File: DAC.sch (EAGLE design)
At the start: 89 parts, among them IC1 LM2662, IC2 PCM1793, IC3 OPA2134PA, IC4 LMH6643, J1 USBSMD, J2 RCJ-21XXMILL, U1 LDO-TPS78233, U2 PCM2707, Y1 12MHz/20pF

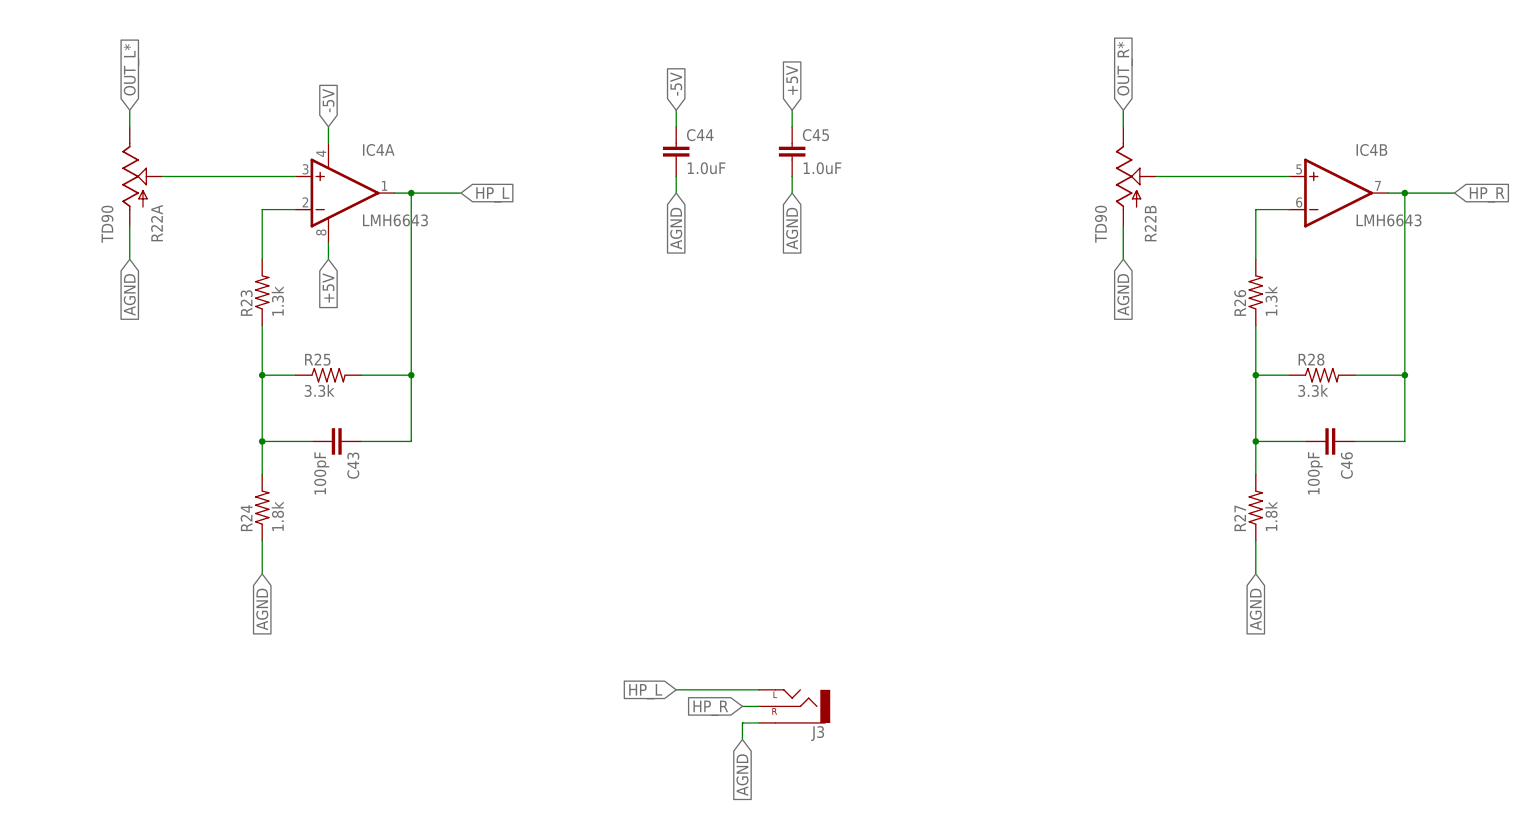
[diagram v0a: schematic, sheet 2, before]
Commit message: More decoupling
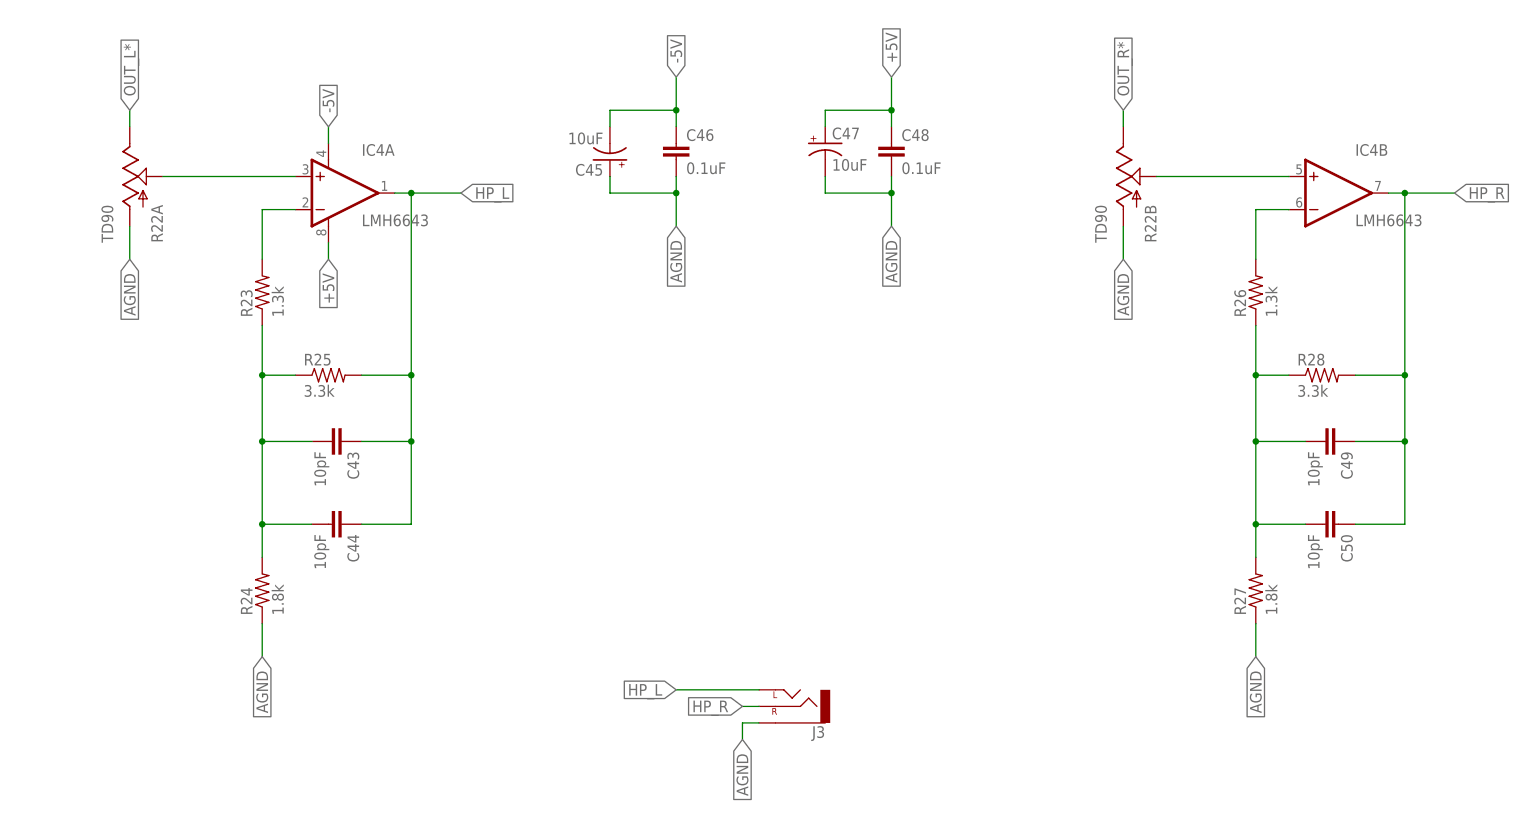
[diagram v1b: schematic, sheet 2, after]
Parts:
- added C47: 10uF, SparkFun-Capacitors:CAP_POLPTH2
- added C48: 0.1uF, SparkFun-Capacitors:1.0UF-16V-10%(0603)
- added C49: 10pF, SparkFun-Capacitors:CAPPTH
- added C50: 10pF, SparkFun-Capacitors:10PF-50V-5%(0603)
- C43: value 100pF -> 10pF
- C44: value 1.0uF -> 10pF; device SparkFun-Capacitors:1.0UF-16V-10%(0603) -> SparkFun-Capacitors:10PF-50V-5%(0603)
- C45: value 1.0uF -> 10uF; device SparkFun-Capacitors:1.0UF-16V-10%(0603) -> SparkFun-Capacitors:CAP_POLPTH2
- C46: value 100pF -> 0.1uF; device SparkFun-Capacitors:CAPPTH -> SparkFun-Capacitors:1.0UF-16V-10%(0603)
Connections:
- net +5V: now also C47.+, C48.1; no longer C45.1
- net -5V: now also C45.-, C46.1; no longer C44.1
- net AGND: now also C45.+, C46.2, C47.-, C48.2; no longer C44.2, C45.2
- net HP_L: now also C44.1
- net HP_R: now also C49.1, C50.1; no longer C46.1
- net N$14: now also C44.2
- net N$19: now also C49.2, C50.2; no longer C46.2
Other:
- note added: "Optional"
- moved on the sheet: C44, C46, R24, R27

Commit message: Caps footprint changed to more standard
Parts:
- C18, C21, C22, C6: device rcl:CPOL-USE3.5-8 -> my-cap:CAP_POLPTH8MM
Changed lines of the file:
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@@
 <attribute name="MOUSER_ID" value=" 652-SRN6045-101M"/>
 </part>
-<part name="C21" library="rcl" deviceset="CPOL-US" device="E3.5-8" value="220uF">
+<part name="C21" library="my-cap" deviceset="CAP_POL" device="PTH8MM" value="220uF">
 <attribute name="PACKAGE" value="8/3.5"/>
 </part>
@@
 <part name="C15" library="SparkFun-Capacitors" deviceset="0.1UF-25V-5%(0603)" device="" value="0.1uF"/>
 <part name="GND17" library="SparkFun-Aesthetics" deviceset="GND" device=""/>
-<part name="C6" library="rcl" deviceset="CPOL-US" device="E3.5-8" value="220uF/Low ESR"/>
+<part name="C6" library="my-cap" deviceset="CAP_POL" device="PTH8MM" value="220uF/Low ESR"/>
 <part name="J1" library="SparkFun-Connectors" deviceset="USB" device="SMD"/>
 <part name="GND21" library="SparkFun-Aesthetics" deviceset="GND" device=""/>
 <part name="SUPPLY2" library="SparkFun-Aesthetics" deviceset="VCC" device=""/>
-<part name="C18" library="rcl" deviceset="CPOL-US" device="E3.5-8" value="220uF/Low ESR"/>
+<part name="C18" library="my-cap" deviceset="CAP_POL" device="PTH8MM" value="220uF/Low ESR"/>
 <part name="C4" library="SparkFun-Capacitors" deviceset="1.0UF-16V-10%(0603)" device="" value="1.0uF"/>
 <part name="C14" library="SparkFun-Capacitors" deviceset="1.0UF-16V-10%(0603)" device="" value="1.0uF"/>
@@
 </part>
 <part name="C19" library="SparkFun-Capacitors" deviceset="1.0UF-16V-10%(0603)" device="" value="1.0uF"/>
-<part name="C22" library="rcl" deviceset="CPOL-US" device="E3.5-8" value="220uF">
+<part name="C22" library="my-cap" deviceset="CAP_POL" device="PTH8MM" value="220uF">
 <attribute name="PACKAGE" value="8/3.5"/>
 </part>

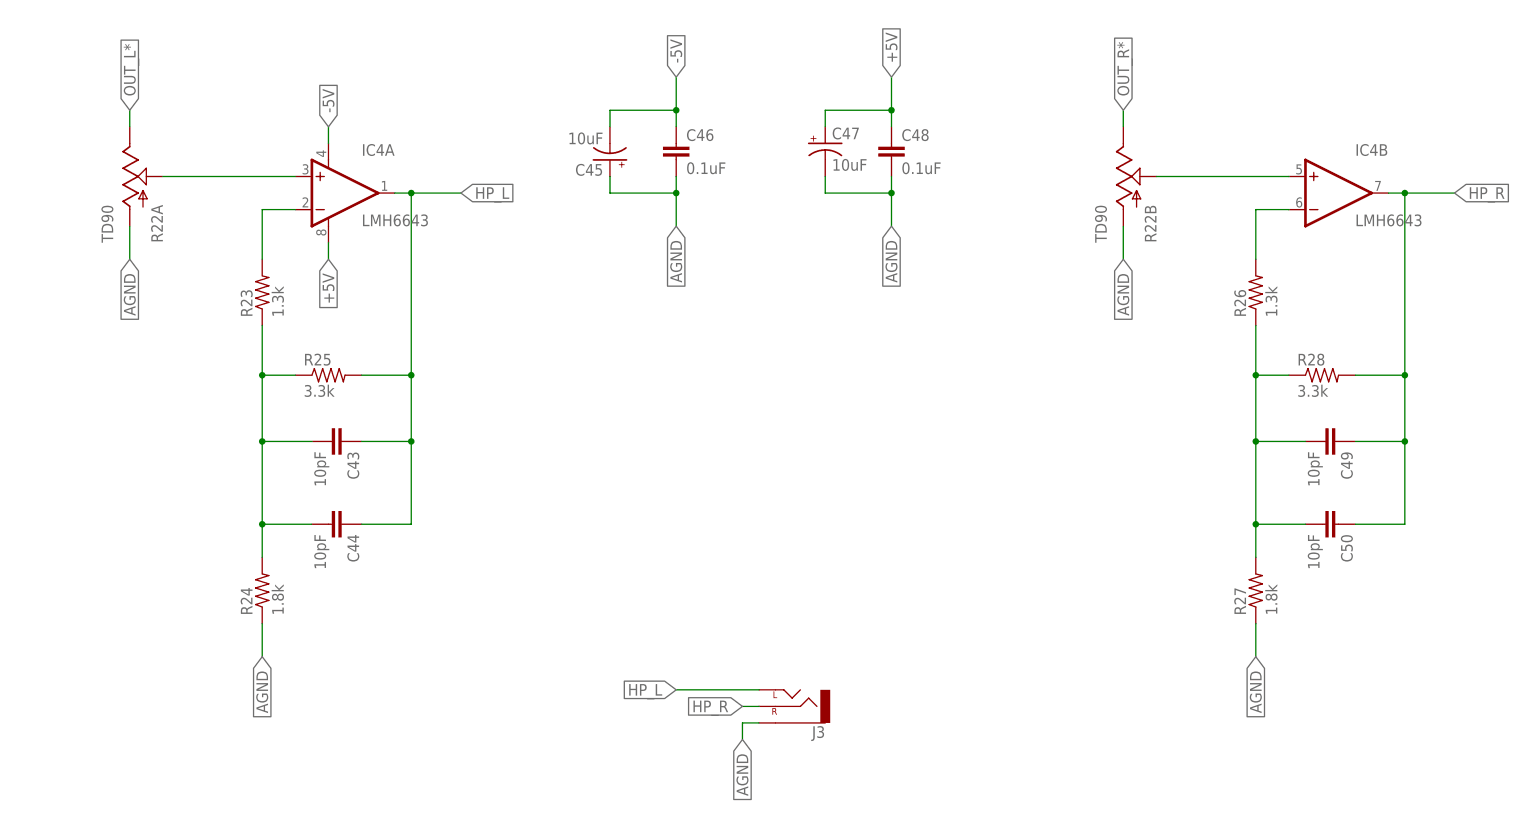
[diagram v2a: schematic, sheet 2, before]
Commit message: Power op amp is AC coupled now to avoid bias current to pass through the pot
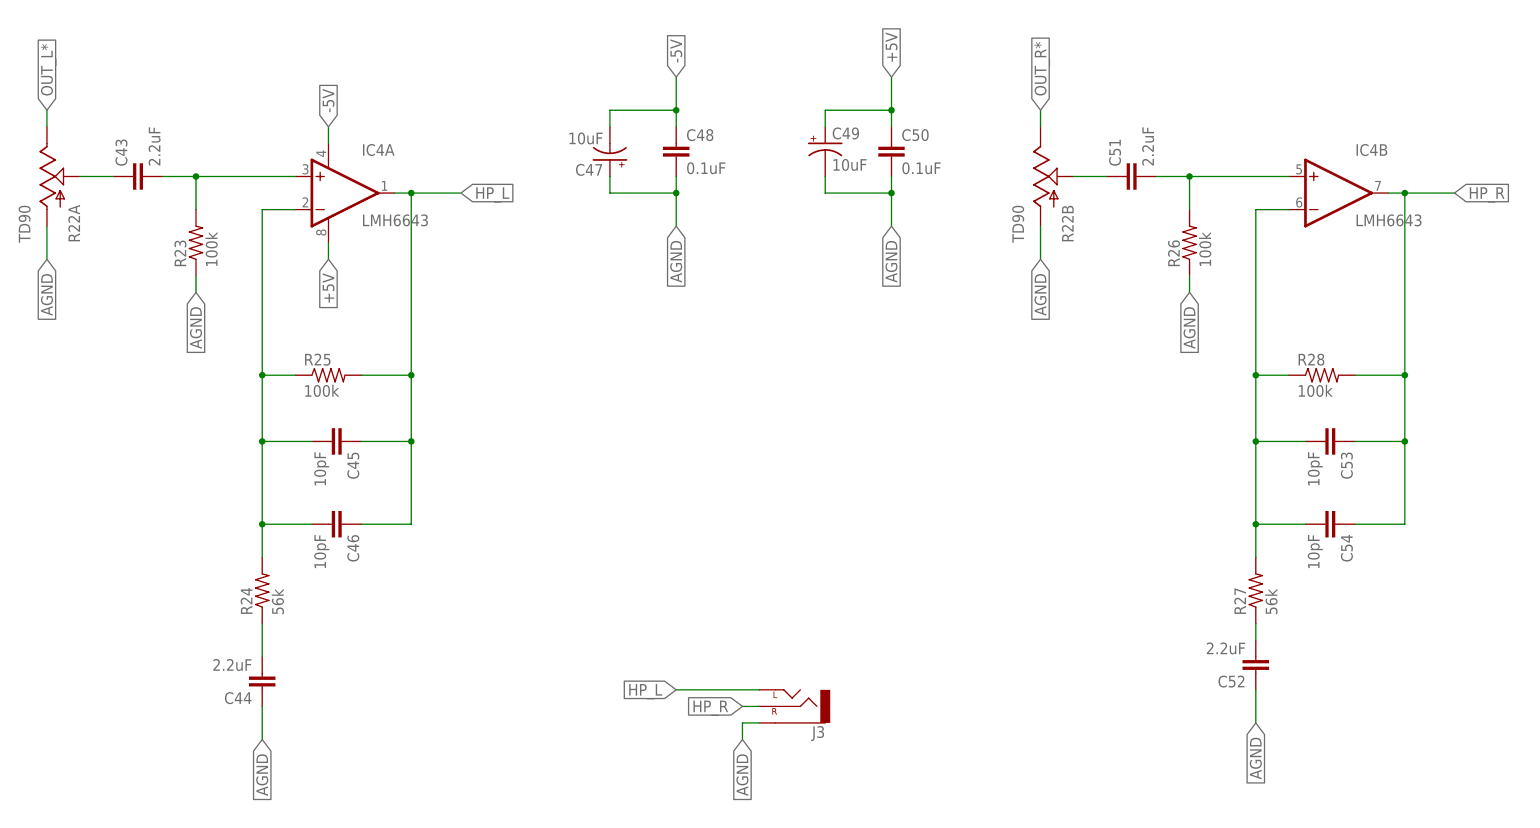
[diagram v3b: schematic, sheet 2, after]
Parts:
- added C51, C52: 2.2uF, capacitor-wima:C5/5
- added C53: 10pF, SparkFun-Capacitors:CAPPTH
- added C54: 10pF, SparkFun-Capacitors:10PF-50V-5%(0603)
- C43: value 10pF -> 2.2uF; device SparkFun-Capacitors:CAPPTH -> capacitor-wima:C5/5
- C44: value 10pF -> 2.2uF; device SparkFun-Capacitors:10PF-50V-5%(0603) -> capacitor-wima:C5/5
- C45: value 10uF -> 10pF; device SparkFun-Capacitors:CAP_POLPTH2 -> SparkFun-Capacitors:CAPPTH
- C46: value 0.1uF -> 10pF; device SparkFun-Capacitors:1.0UF-16V-10%(0603) -> SparkFun-Capacitors:10PF-50V-5%(0603)
- C49: value 10pF -> 10uF; device SparkFun-Capacitors:CAPPTH -> SparkFun-Capacitors:CAP_POLPTH2
- C50: value 10pF -> 0.1uF; device SparkFun-Capacitors:10PF-50V-5%(0603) -> SparkFun-Capacitors:1.0UF-16V-10%(0603)
- R23, R26: value 1.3k -> 100k
- R24, R27: value 1.8k -> 56k
- R25, R28: value 3.3k -> 100k
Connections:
- removed net N$6: IC4B.-IN, R26.2
- new net N$23: C43.1, R22A.S
- new net N$24: C52.2, R27.1
- new net N$25: C44.2, R24.1
- net +5V: now also C49.+, C50.1; no longer C47.+, C48.1
- net -5V: now also C47.-, C48.1; no longer C45.-, C46.1
- net AGND: now also C44.1, C47.+, C49.-, C50.2, C52.1, R23.1, R26.1; no longer C45.+, C46.2, C47.-, R24.1, R27.1
- net HP_L: now also C45.1, C46.1; no longer C43.1, C44.1
- net HP_R: now also C53.1, C54.1; no longer C49.1, C50.1
- net N$12: now also C43.2, R23.2; no longer R22A.S
- net N$14: now also C51.1, R22B.S; no longer C43.2, C44.2, R23.1, R24.2, R25.1
- net N$15: now also C51.2, R26.2; no longer R22B.S
- net N$19: now also C53.2, C54.2, IC4B.-IN; no longer C49.2, C50.2, R26.1
- net N$7: now also C45.2, C46.2, R24.2, R25.1; no longer R23.2
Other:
- moved on the sheet: C43, C44, C46, C47, C48, C50, R22A, R22B, R23, R26

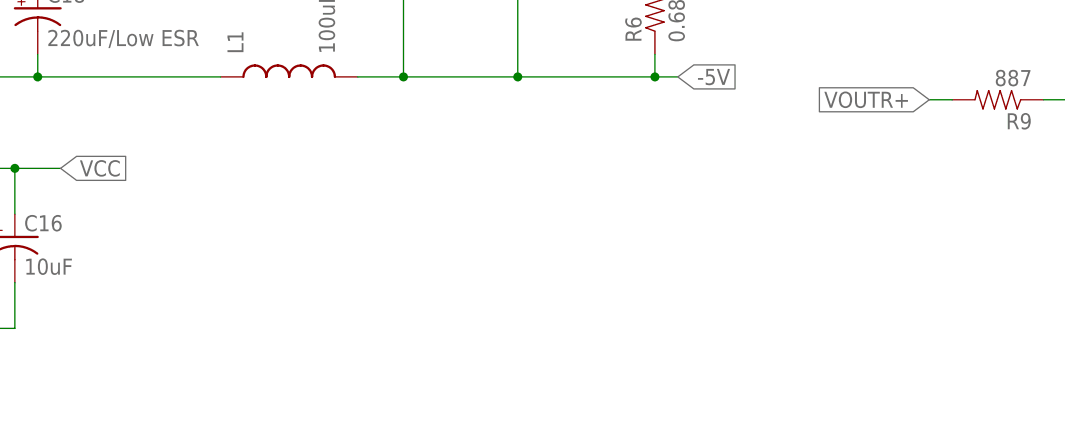
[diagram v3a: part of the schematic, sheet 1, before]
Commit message: Mounting holes
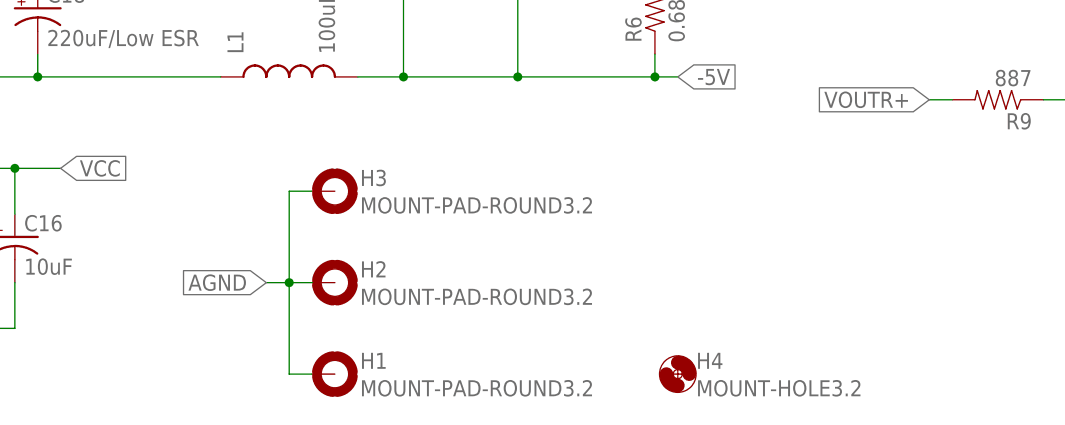
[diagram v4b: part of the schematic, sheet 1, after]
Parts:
- added H1, H2, H3: MOUNT-PAD-ROUND3.2, holes:MOUNT-PAD-ROUND3.2
- added H4: MOUNT-HOLE3.2, holes:MOUNT-HOLE3.2
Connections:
- net AGND: now also H1.MOUNT, H2.MOUNT, H3.MOUNT
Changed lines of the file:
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@@
 <part name="C44" library="capacitor-wima" deviceset="C" device="5/5" value="2.2uF"/>
 <part name="C52" library="capacitor-wima" deviceset="C" device="5/5" value="2.2uF"/>
+<part name="H1" library="holes" deviceset="MOUNT-PAD-ROUND" device="3.2"/>
+<part name="H2" library="holes" deviceset="MOUNT-PAD-ROUND" device="3.2"/>
+<part name="H3" library="holes" deviceset="MOUNT-PAD-ROUND" device="3.2"/>
+<part name="H4" library="holes" deviceset="MOUNT-HOLE" device="3.2"/>
 </parts>
 <sheets>
@@
 <instance part="R20" gate="G$1" x="307.34" y="111.76"/>
 <instance part="LOGO1" gate="G$1" x="363.22" y="30.48"/>
+<instance part="H1" gate="G$1" x="152.4" y="12.7"/>
+<instance part="H2" gate="G$1" x="152.4" y="22.86"/>
+<instance part="H3" gate="G$1" x="152.4" y="33.02"/>
+<instance part="H4" gate="G$1" x="190.5" y="12.7"/>
 </instances>
 <busses>
@@
 <label x="330.2" y="132.08" size="1.778" layer="95" rot="R270" xref="yes"/>
 </segment>
-</net>
+<segment>
+<pinref part="H3" gate="G$1" pin="MOUNT"/>
+<wire x1="149.86" y1="33.02" x2="147.32" y2="33.02" width="0.1524" layer="91"/>
+<wire x1="147.32" y1="33.02" x2="147.32" y2="22.86" width="0.1524" layer="91"/>
+<pinref part="H1" gate="G$1" pin="MOUNT"/>
+<wire x1="147.32" y1="22.86" x2="147.32" y2="12.7" width="0.1524" layer="91"/>
+<wire x1="149.86" y1="12.7" x2="147.32" y2="12.7" width="0.1524" layer="91"/>
+<pinref part="H2" gate="G$1" pin="MOUNT"/>
+<wire x1="149.86" y1="22.86" x2="147.32" y2="22.86" width="0.1524" layer="91"/>
+<junction x="147.32" y="22.86"/>
+<wire x1="147.32" y1="22.86" x2="144.78" y2="22.86" width="0.1524" layer="91"/>
+<label x="144.78" y="22.86" size="1.778" layer="95" rot="R180" xref="yes"/>
+</segment>
+</net>
